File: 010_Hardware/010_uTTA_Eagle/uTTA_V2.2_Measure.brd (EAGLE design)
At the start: 100.4 x 79 mm, 287 parts, among them IC101.1 LT1167, IC101.2 LT1167, IC101.3 LT1167, IC101.4 LT1167, IC151.1 MCP602SN, IC151.3 MCP602SN, IC301 AD5664, IC302 LT1004CLP-2.5, IC303 TL074D, IC351.1 AD8672ARZ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

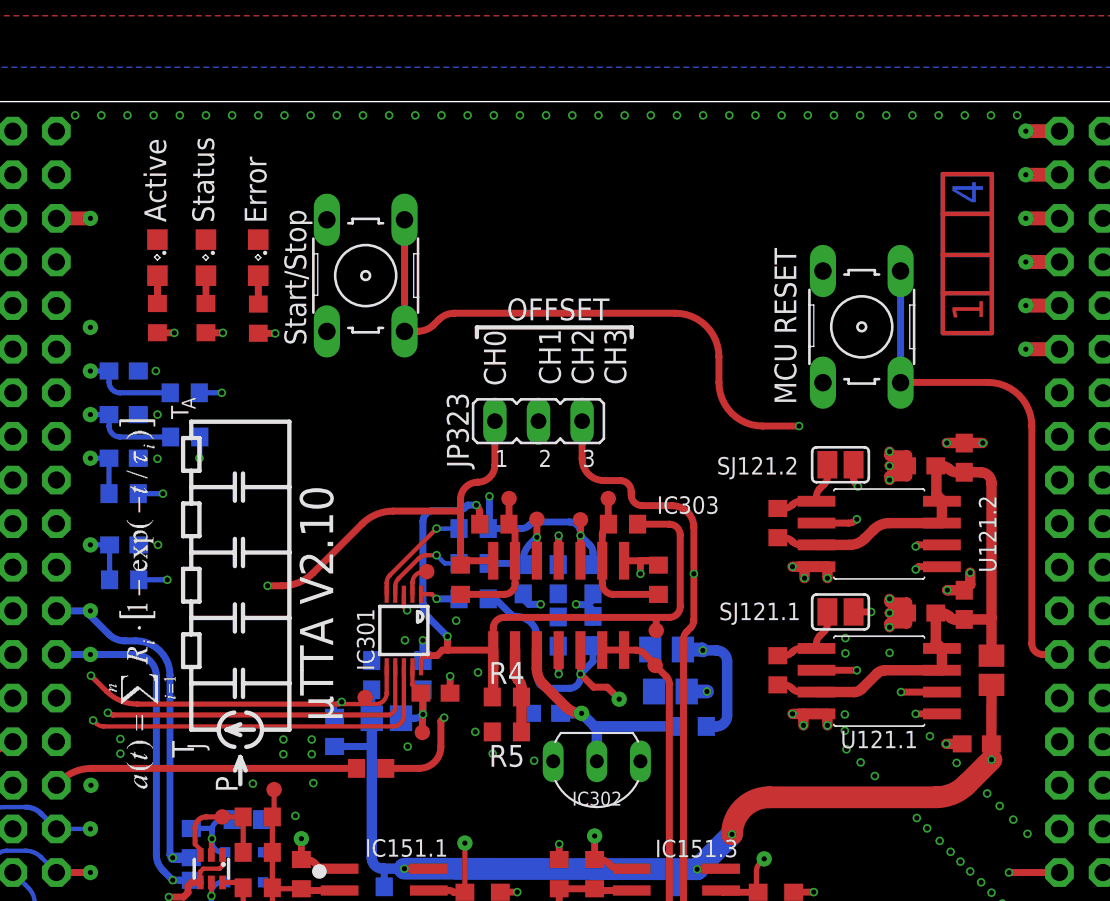
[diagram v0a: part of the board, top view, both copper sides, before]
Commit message: Update to uTTA Version 2.2
Full update of both PCBs to HW Version 2.2:
Removed spare FLASH Memory
Adjusted Position of LEDs and Buttons
Cleanup of layout
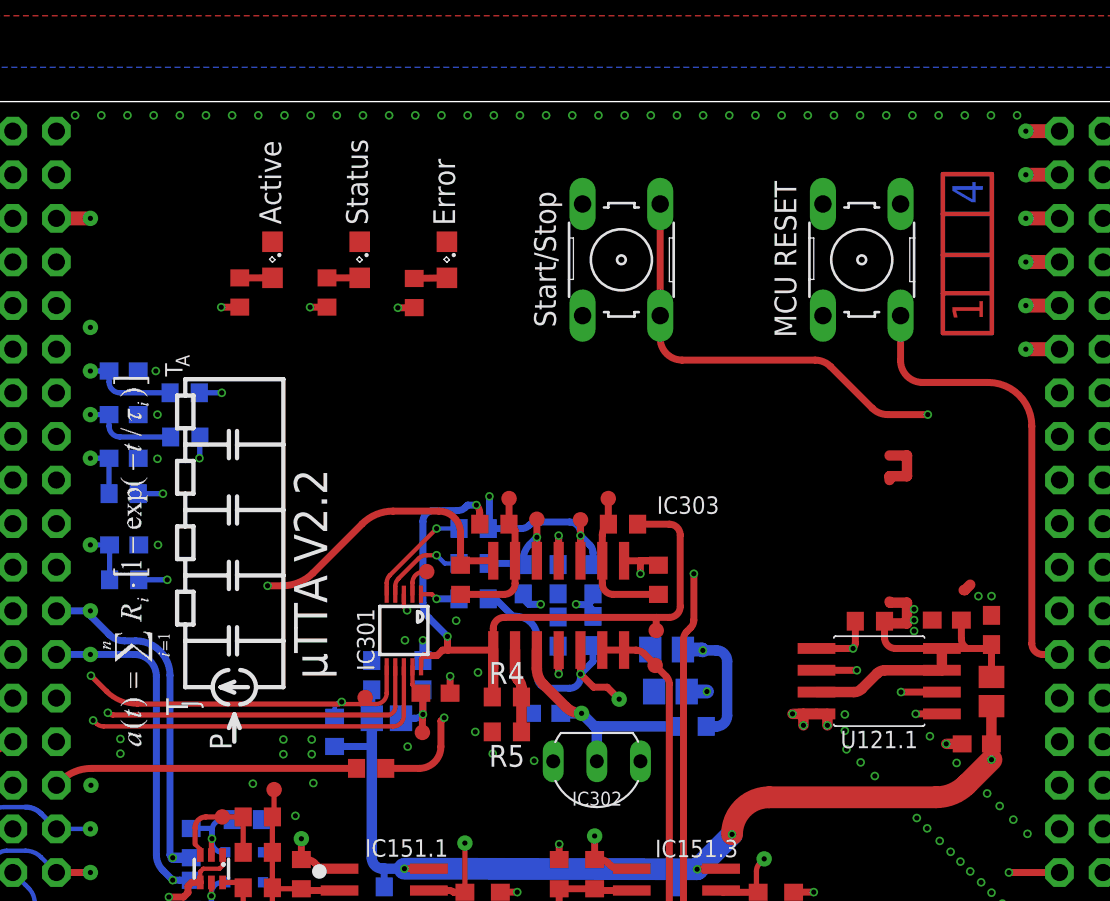
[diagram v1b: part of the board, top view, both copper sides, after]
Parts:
- removed C122.2: 1u/25V, A_Kondensatoren:C0603
- removed C123.2: 100n/50V, A_Kondensatoren:C0603
- removed JP323: (no value), Connectors jumper:JP2
- removed R121.2: 10k, A_Resistor:R0603
- removed SJ121.1, SJ121.2: (no value), jumper:SJ
- removed U121.2: W25Q128JV, XMC4500_Relax-V1:SO08W
- C107.1, C107.2, C107.3, C107.4: value 100n/50V -> DNP
- moved S1 14.9 mm to (-132.6, 71.4)
- moved LED1 11.0 mm to (-142.7, 71.4)
- moved R1 9.20 mm to (-144.6, 69.4)
- moved LED3 8.95 mm to (-147.8, 71.4)
- moved R3 7.20 mm to (-149.7, 69.5)
- moved LED2 6.70 mm to (-152.9, 71.4)
- moved R121.1 6.08 mm to (-118.1, 50.3), turned to 180 degrees
- moved R2 5.02 mm to (-154.8, 69.5)
- moved S11 3.91 mm to (-118.6, 71.4)
- moved C122.1 2.16 mm to (-111.0, 49.8)
- moved C123.1 1.55 mm to (-113.6, 50.4)
- moved L121 1.24 mm to (-111.0, 46.2)
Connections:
- removed net !FLASH1_SPI_CSN: R121.1.2, SJ121.1.2, U121.1.1
- removed net !FLASH2_SPI_CSN: R121.2.2, SJ121.2.2, U121.2.1
- net !FLASH_SPI_CSN_DO: now also R121.1.2, U121.1.1; no longer SJ121.1.1, SJ121.2.1
- net +5V/4: no longer C122.2.1, C123.2.1, R121.2.1, U121.2.3, U121.2.7, U121.2.8
- net AGND: no longer C122.2.2, C123.2.2, JP323.2, U121.2.4
- net FLASH_SPI_MISO_DI: no longer U121.2.2
- net FLASH_SPI_MOSI_DO: no longer U121.2.5
- net FLASH_SPI_SCK_DO: no longer U121.2.6
- net V_OFF0: no longer JP323.1
- net V_OFF1_3: no longer JP323.3
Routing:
- net +5V/4: track 44.1 -> 20.1 mm
- net B1_BUTTON_DI: track 51.6 -> 35.8 mm
- net V_OFF1_3: track 80.0 -> 66.8 mm
- net FLASH_SPI_MISO_DI: track 33.5 -> 22.4 mm, vias 2 -> 1
- net FLASH_SPI_SCK_DO: track 31.9 -> 21.4 mm, vias 2 -> 1
- net FLASH_SPI_MOSI_DO: track 27.0 -> 16.9 mm, vias 2 -> 1
- net AGND: track 59.7 -> 49.8 mm, vias 309 -> 298
- net !FLASH_SPI_CSN_DO: track 31.3 -> 23.7 mm, vias 3 -> 2
- net V_OFF0: track 53.4 -> 46.6 mm
- net TIM4_CH4_DO: track 17.7 -> 24.3 mm
- net !FLASH1_SPI_CSN: track 4.66 -> 0.00 mm
- net !FLASH2_SPI_CSN: track 4.66 -> 0.00 mm
- net TIM4_CH4_DO2: track 11.7 -> 16.1 mm
- net RESET: track 29.7 -> 26.4 mm
- net TIM4_CH4_DO1: track 11.9 -> 14.1 mm
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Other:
- board text added: "µTTA V2.2"
- board text removed: "CH1 CH2 CH3"
- board text removed: "OFFSET"
- board text removed: "µTTA V2.10"

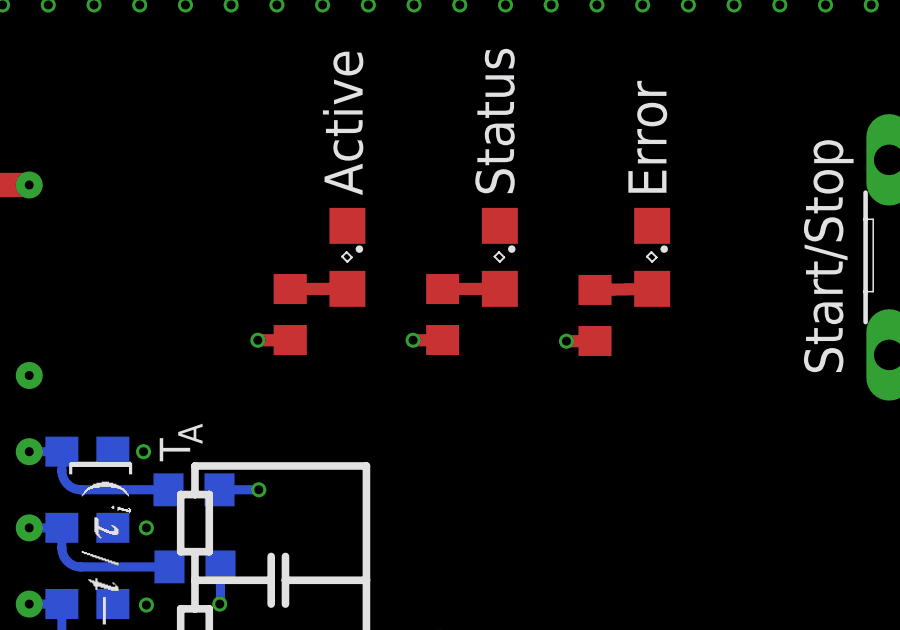
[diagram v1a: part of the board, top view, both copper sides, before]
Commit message: Swapped LEDs LED1 and LED3 because of twisted naming
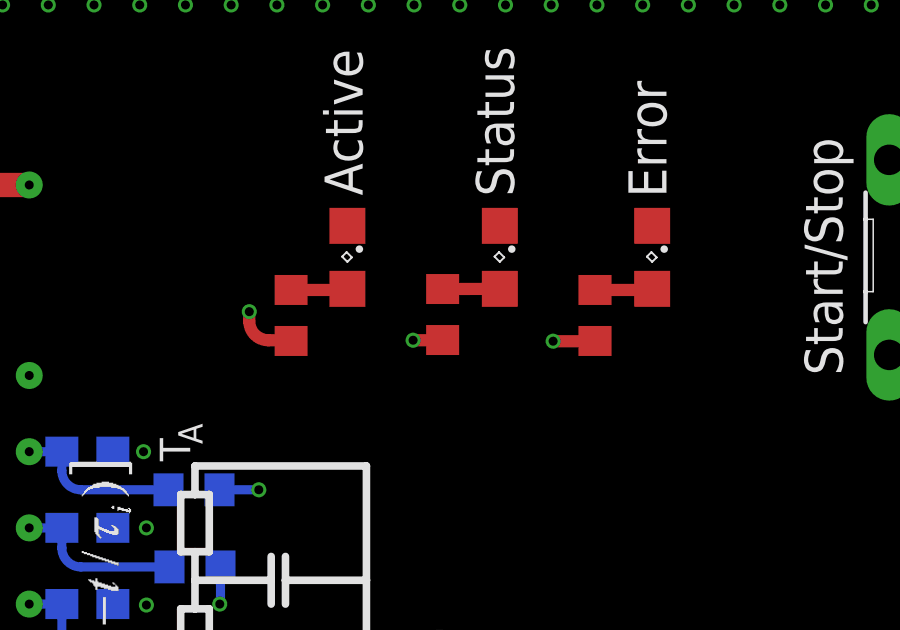
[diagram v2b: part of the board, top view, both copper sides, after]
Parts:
- moved R2 10.2 mm to (-144.6, 69.4)
- moved LED1 10.2 mm to (-152.9, 71.4)
- moved LED2 10.2 mm to (-142.7, 71.4)
- moved R1 10.1 mm to (-154.7, 69.4)
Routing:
- net TIM4_CH4_DO1: track 14.1 -> 24.6 mm
- net TIM4_CH4_DO: track 24.3 -> 14.6 mm
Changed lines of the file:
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@@
 <variant name="Controller Adjust" populate="no"/>
 </element>
-<element name="R1" library="A_Resistor" package="R0603" value="680" x="-144.62125" y="69.43725" smashed="yes" rot="R90">
-<attribute name="PACKAGE" value="R0603" x="-149.82825" y="69.43725" size="1.778" layer="27" rot="R90" display="off"/>
-<attribute name="NAME" x="-144.62125" y="69.43725" size="0.4064" layer="37" font="vector" rot="R90" align="center"/>
-<attribute name="VALUE" x="-143.22425" y="69.43725" size="1.27" layer="27" font="vector" rot="R90" align="center"/>
+<element name="R1" library="A_Resistor" package="R0603" value="680" x="-154.7495" y="69.43725" smashed="yes" rot="R90">
+<attribute name="PACKAGE" value="R0603" x="-159.9565" y="69.43725" size="1.778" layer="27" rot="R90" display="off"/>
+<attribute name="NAME" x="-154.7495" y="69.43725" size="0.4064" layer="37" font="vector" rot="R90" align="center"/>
+<attribute name="VALUE" x="-153.3525" y="69.43725" size="1.27" layer="27" font="vector" rot="R90" align="center"/>
 </element>
-<element name="LED1" library="A_LED" package="SML0805" value="GREEN" x="-142.71625" y="71.374" smashed="yes" rot="R270">
-<attribute name="VALUE" x="-144.71625" y="72.874" size="1.27" layer="27" rot="R270"/>
-<attribute name="NAME" x="-142.71625" y="71.374" size="0.6096" layer="37" rot="R270" align="center"/>
+<element name="LED1" library="A_LED" package="SML0805" value="GREEN" x="-152.87625" y="71.374" smashed="yes" rot="R270">
+<attribute name="VALUE" x="-154.87625" y="72.874" size="1.27" layer="27" rot="R270"/>
+<attribute name="NAME" x="-152.87625" y="71.374" size="0.6096" layer="37" rot="R270" align="center"/>
 </element>
 <element name="S1" library="switch-omron" package="B3F-10XX" value="" x="-132.5545" y="71.374" smashed="yes" rot="R270">
@@
 <attribute name="VALUE" x="-137.6345" y="74.422" size="1.27" layer="27" ratio="10" rot="R270"/>
 </element>
-<element name="R2" library="A_Resistor" package="R0603" value="680" x="-154.78125" y="69.469" smashed="yes" rot="R90">
-<attribute name="PACKAGE" value="R0603" x="-159.98825" y="69.469" size="1.778" layer="27" rot="R90" display="off"/>
-<attribute name="NAME" x="-154.78125" y="69.469" size="0.4064" layer="37" font="vector" rot="R90" align="center"/>
-<attribute name="VALUE" x="-153.38425" y="69.469" size="1.27" layer="27" font="vector" rot="R90" align="center"/>
+<element name="R2" library="A_Resistor" package="R0603" value="680" x="-144.62125" y="69.43725" smashed="yes" rot="R90">
+<attribute name="PACKAGE" value="R0603" x="-149.82825" y="69.43725" size="1.778" layer="27" rot="R90" display="off"/>
+<attribute name="NAME" x="-144.62125" y="69.43725" size="0.4064" layer="37" font="vector" rot="R90" align="center"/>
+<attribute name="VALUE" x="-143.22425" y="69.43725" size="1.27" layer="27" font="vector" rot="R90" align="center"/>
 </element>
-<element name="LED2" library="A_LED" package="SML0805" value="RED" x="-152.87625" y="71.374" smashed="yes" rot="R270">
-<attribute name="VALUE" x="-154.87625" y="72.874" size="1.27" layer="27" rot="R270"/>
-<attribute name="NAME" x="-152.87625" y="71.374" size="0.6096" layer="37" rot="R270" align="center"/>
+<element name="LED2" library="A_LED" package="SML0805" value="RED" x="-142.71625" y="71.374" smashed="yes" rot="R270">
+<attribute name="VALUE" x="-144.71625" y="72.874" size="1.27" layer="27" rot="R270"/>
+<attribute name="NAME" x="-142.71625" y="71.374" size="0.6096" layer="37" rot="R270" align="center"/>
 </element>
 <element name="R3" library="A_Resistor" package="R0603" value="680" x="-149.70125" y="69.469" smashed="yes" rot="R90">
@@
 <wire x1="-163.48075" y1="73.787" x2="-163.48075" y2="71.64605" width="0.4064" layer="15"/>
 <wire x1="-163.48075" y1="71.64605" x2="-163.108775" y2="70.748025" width="0.4064" layer="15" curve="45"/>
-<via x="-145.57375" y="68.58" extent="1-16" drill="0.3"/>
-<wire x1="-145.57375" y1="68.58" x2="-144.614" y2="68.58" width="0.4064" layer="1"/>
-<wire x1="-144.614" y1="68.58" x2="-144.62125" y2="68.58725" width="0.4064" layer="1"/>
 <wire x1="-163.108775" y1="70.748025" x2="-162.042975" y2="69.682225" width="0.4064" layer="15"/>
 <wire x1="-162.042975" y1="69.682225" x2="-161.14495" y2="69.31025" width="0.4064" layer="15" curve="45"/>
-<wire x1="-161.14495" y1="69.31025" x2="-148.6398" y2="69.31025" width="0.4064" layer="15"/>
-<wire x1="-148.6398" y1="69.31025" x2="-147.741775" y2="68.938275" width="0.4064" layer="15" curve="-45"/>
-<wire x1="-147.741775" y1="68.938275" x2="-147.6375" y2="68.834" width="0.4064" layer="15"/>
-<wire x1="-147.6375" y1="68.834" x2="-147.024290625" y2="68.58" width="0.4064" layer="15" curve="45"/>
-<wire x1="-147.024290625" y1="68.58" x2="-145.57375" y2="68.58" width="0.4064" layer="15"/>
+<wire x1="-161.14495" y1="69.31025" x2="-156.663525" y2="69.31025" width="0.4064" layer="15"/>
+<wire x1="-156.663525" y1="69.31025" x2="-156.2145125" y2="69.4962375" width="0.4064" layer="15" curve="45"/>
+<wire x1="-156.2145125" y1="69.4962375" x2="-156.1465" y2="69.56425" width="0.4064" layer="15"/>
+<via x="-156.1465" y="69.56425" extent="1-16" drill="0.3"/>
+<wire x1="-156.1465" y1="69.56425" x2="-156.1465" y2="69.24675" width="0.4064" layer="1"/>
+<wire x1="-156.1465" y1="69.24675" x2="-155.5115" y2="68.61175" width="0.4064" layer="1" curve="90"/>
+<wire x1="-155.5115" y1="68.61175" x2="-154.774" y2="68.61175" width="0.4064" layer="1"/>
+<wire x1="-154.774" y1="68.61175" x2="-154.7495" y2="68.58725" width="0.4064" layer="1"/>
 </signal>
 <signal name="SWO">
@@
 <contactref element="R1" pad="2"/>
 <contactref element="LED1" pad="A"/>
-<wire x1="-144.62125" y1="70.28725" x2="-142.71625" y2="70.324" width="0.4064" layer="1"/>
+<wire x1="-154.7495" y1="70.28725" x2="-152.913" y2="70.28725" width="0.4064" layer="1"/>
+<wire x1="-152.913" y1="70.28725" x2="-152.87625" y2="70.324" width="0.4064" layer="1"/>
 </signal>
 <signal name="TIM4_CH4_DO1" class="2">
@@
 <wire x1="-164.465" y1="70.00875" x2="-163.91155" y2="70.00875" width="0.4064" layer="15"/>
 <wire x1="-163.91155" y1="70.00875" x2="-163.013525" y2="69.636775" width="0.4064" layer="15" curve="-45"/>
-<via x="-155.86075" y="68.61175" extent="1-16" drill="0.3"/>
-<wire x1="-155.86075" y1="68.61175" x2="-154.774" y2="68.61175" width="0.4064" layer="1"/>
-<wire x1="-154.774" y1="68.61175" x2="-154.78125" y2="68.619" width="0.4064" layer="1"/>
 <wire x1="-163.013525" y1="69.636775" x2="-162.360475" y2="68.983725" width="0.4064" layer="15"/>
 <wire x1="-162.360475" y1="68.983725" x2="-161.46245" y2="68.61175" width="0.4064" layer="15" curve="45"/>
-<wire x1="-161.46245" y1="68.61175" x2="-155.86075" y2="68.61175" width="0.4064" layer="15"/>
+<wire x1="-161.46245" y1="68.61175" x2="-153.8468" y2="68.61175" width="0.4064" layer="15"/>
+<wire x1="-153.8468" y1="68.61175" x2="-152.948775" y2="68.983725" width="0.4064" layer="15" curve="45"/>
+<wire x1="-152.948775" y1="68.983725" x2="-152.930725" y2="69.001775" width="0.4064" layer="15"/>
+<wire x1="-152.930725" y1="69.001775" x2="-152.0327" y2="69.37375" width="0.4064" layer="15" curve="-45"/>
+<wire x1="-152.0327" y1="69.37375" x2="-147.59205" y2="69.37375" width="0.4064" layer="15"/>
+<wire x1="-147.59205" y1="69.37375" x2="-146.694025" y2="69.001775" width="0.4064" layer="15" curve="-45"/>
+<wire x1="-146.694025" y1="69.001775" x2="-146.45185625" y2="68.75960625" width="0.4064" layer="15"/>
+<wire x1="-146.45185625" y1="68.75960625" x2="-146.01825" y2="68.58" width="0.4064" layer="15" curve="45"/>
+<via x="-146.01825" y="68.58" extent="1-16" drill="0.3"/>
+<wire x1="-146.01825" y1="68.58" x2="-144.6285" y2="68.58" width="0.4064" layer="1"/>
+<wire x1="-144.6285" y1="68.58" x2="-144.62125" y2="68.58725" width="0.4064" layer="1"/>
 </signal>
 <signal name="N$4" class="2">
 <contactref element="R2" pad="2"/>
 <contactref element="LED2" pad="A"/>
-<wire x1="-154.78125" y1="70.319" x2="-152.87625" y2="70.324" width="0.4064" layer="1"/>
+<wire x1="-144.62125" y1="70.28725" x2="-142.753" y2="70.28725" width="0.4064" layer="1"/>
+<wire x1="-142.753" y1="70.28725" x2="-142.71625" y2="70.324" width="0.4064" layer="1"/>
 </signal>
 <signal name="TIM4_CH4_DO2" class="2">

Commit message: removed outdated variants from design
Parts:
- R302: value 1k -> 10k
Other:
- board size 100.4 x 79 mm -> 100.4 x 83.4 mm
- board text added: ">VERSION"
- board text added: "µTTA"
- board text removed: "µTTA V2.2"
